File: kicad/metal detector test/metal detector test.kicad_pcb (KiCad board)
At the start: 2 copper layers, 0 parts

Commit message: Starting PCB layout.  Also added alternate MPNs for a few more regulators sampled from TI
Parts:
- added BT1: 12V (18650 x3), Connector_PinHeader_2.54mm:PinHeader_1x02_P2.54mm_Vertical, F.Cu at (137.2, 95.9)
- added C1: 100u, Capacitor_SMD:C_1206_3216Metric_Pad1.33x1.80mm_HandSolder, F.Cu at (74.0, 122.0)
- added C10: 100n, Capacitor_SMD:C_0805_2012Metric_Pad1.18x1.45mm_HandSolder, F.Cu at (143.5, 95.2)
- added C11: 3.3u, Capacitor_SMD:C_0805_2012Metric_Pad1.18x1.45mm_HandSolder, F.Cu at (151.1, 95.2)
- added C12: 10u, Capacitor_SMD:C_1206_3216Metric_Pad1.33x1.80mm_HandSolder, F.Cu at (135.9, 99.1)
- added C13: 100n, Capacitor_SMD:C_0805_2012Metric_Pad1.18x1.45mm_HandSolder, F.Cu at (201.0, 90.5)
- added C14: 100n, Capacitor_SMD:C_0805_2012Metric_Pad1.18x1.45mm_HandSolder, F.Cu at (197.2, 98.7)
- added C15: 1000u, Capacitor_THT:CP_Radial_D10.0mm_P5.00mm, F.Cu at (192.6, 111.4)
- added C16: 100n, Capacitor_SMD:C_0805_2012Metric_Pad1.18x1.45mm_HandSolder, F.Cu at (192.3, 101.9)
- added C17: 100u, Capacitor_SMD:C_1206_3216Metric_Pad1.33x1.80mm_HandSolder, F.Cu at (201.0, 100.0)
- added C18: 100n, Capacitor_SMD:C_0805_2012Metric_Pad1.18x1.45mm_HandSolder, F.Cu at (194.6, 90.5)
- added C19: .33u, Capacitor_SMD:C_0805_2012Metric_Pad1.18x1.45mm_HandSolder, F.Cu at (137.2, 103.5)
- added C2: 470n, Capacitor_SMD:C_1206_3216Metric_Pad1.33x1.80mm_HandSolder, F.Cu at (149.2, 121.9)
- added C20: 100n, Capacitor_SMD:C_0805_2012Metric_Pad1.18x1.45mm_HandSolder, F.Cu at (143.5, 106.7)
- added C21: 3.3u, Capacitor_SMD:C_0805_2012Metric_Pad1.18x1.45mm_HandSolder, F.Cu at (151.1, 106.7)
- added C22: 1000u, Capacitor_THT:CP_Radial_D10.0mm_P5.00mm, F.Cu at (205.0, 96.2)
- added C23: 100n, Capacitor_SMD:C_0805_2012Metric_Pad1.18x1.45mm_HandSolder, F.Cu at (158.1, 156.2)
- added C24: 100n, Capacitor_SMD:C_0805_2012Metric_Pad1.18x1.45mm_HandSolder, F.Cu at (209.9, 103.2)
- added C25: 1000u, Capacitor_THT:CP_Radial_D10.0mm_P5.00mm, F.Cu at (213.1, 112.9)
- added C26: 33n, Capacitor_SMD:C_0805_2012Metric_Pad1.18x1.45mm_HandSolder, F.Cu at (154.9, 164.5)
- added C27: 100n, Capacitor_SMD:C_0805_2012Metric_Pad1.18x1.45mm_HandSolder, F.Cu at (209.9, 106.4)
- added C28: 100n, Capacitor_SMD:C_0805_2012Metric_Pad1.18x1.45mm_HandSolder, F.Cu at (164.5, 156.2)
- added C29: 100n, Capacitor_SMD:C_0805_2012Metric_Pad1.18x1.45mm_HandSolder, F.Cu at (166.4, 160.0)
- added C3: 22u, Capacitor_SMD:C_1206_3216Metric_Pad1.33x1.80mm_HandSolder, F.Cu at (149.2, 132.1)
- added C30: 100n, Capacitor_SMD:C_0805_2012Metric_Pad1.18x1.45mm_HandSolder, F.Cu at (166.4, 168.9)
- added C4: 100n, Capacitor_SMD:C_0805_2012Metric_Pad1.18x1.45mm_HandSolder, F.Cu at (115.0, 172.0)
- added C5: 100n, Capacitor_SMD:C_0805_2012Metric_Pad1.18x1.45mm_HandSolder, F.Cu at (75.2, 25.4)
- added C6: 100n, Capacitor_SMD:C_0805_2012Metric_Pad1.18x1.45mm_HandSolder, F.Cu at (77.0, 127.0)
- added C7: 33n, Capacitor_SMD:C_0805_2012Metric_Pad1.18x1.45mm_HandSolder, F.Cu at (110.0, 163.0)
- added C8: 10n, Capacitor_SMD:C_0805_2012Metric_Pad1.18x1.45mm_HandSolder, F.Cu at (103.0, 171.0)
- added C9: .33u, Capacitor_SMD:C_0805_2012Metric_Pad1.18x1.45mm_HandSolder, F.Cu at (137.2, 92.1)
- added DS1: 2.42_inch_128x64_oled, allen footprints:oled_2.42in_128x64, F.Cu at (81.3, 22.9)
- added FB1: ~, Inductor_SMD:L_0805_2012Metric_Pad1.05x1.20mm_HandSolder, F.Cu at (74.9, 27.9)
- added G***: LOGO, LOGO, F.Cu at (36.8, 184.8)
- added H1: MountingHole, MountingHole:MountingHole_3.7mm, F.Cu at (121.9, 55.9)
- added H2: MountingHole, MountingHole:MountingHole_3.7mm, F.Cu at (55.9, 55.9)
- added H3: MountingHole, MountingHole:MountingHole_3.7mm, F.Cu at (55.9, 172.7)
- added H4: MountingHole, MountingHole:MountingHole_3.7mm, F.Cu at (132.1, 188.0)
- added J1: 3.5mm audio jack TRS, allen footprints:SJ-3524-SMT_audio_jack_with_tip_switch_smt, F.Cu at (217.2, 126.7)
- added JP1: SolderJumper_2_Open, Jumper:SolderJumper-2_P1.3mm_Open_Pad1.0x1.5mm, F.Cu at (174.6, 57.8)
- added JP2: SolderJumper_2_Open, Jumper:SolderJumper-2_P1.3mm_Open_Pad1.0x1.5mm, F.Cu at (71.8, 30.5)
- added JP3: SolderJumper_2_Open, Jumper:SolderJumper-2_P1.3mm_Open_Pad1.0x1.5mm, F.Cu at (75.6, 30.5)
- added JP4: SolderJumper_2_Open, Jumper:SolderJumper-2_P1.3mm_Open_Pad1.0x1.5mm, F.Cu at (154.3, 57.8)
- added LS1: Speaker, Connector_PinHeader_2.54mm:PinHeader_1x02_P2.54mm_Vertical, F.Cu at (204.2, 132.4)
- added L_RX1: 6m1, Connector_PinHeader_2.54mm:PinHeader_1x02_P2.54mm_Vertical, F.Cu at (151.8, 163.2)
- added L_TX1: 5m6, Connector_PinHeader_2.54mm:PinHeader_1x02_P2.54mm_Vertical, F.Cu at (105.0, 163.0)
- added L_TX2: 5m6, Connector_PinHeader_2.54mm:PinHeader_1x02_P2.54mm_Vertical, F.Cu at (188.3, 119.7)
- added Q1: ~, allen footprints:SOT-89-3_Handsoldering_allen, F.Cu at (117.0, 158.0)
- added Q2: ~, allen footprints:SOT-89-3_Handsoldering_allen, F.Cu at (117.0, 166.0)
- added R1: 27k, Resistor_SMD:R_0805_2012Metric_Pad1.20x1.40mm_HandSolder, F.Cu at (124.0, 165.0)
- added R10: 33k, Resistor_SMD:R_0805_2012Metric_Pad1.20x1.40mm_HandSolder, F.Cu at (68.0, 78.0)
- added R11: 2k, Resistor_SMD:R_0805_2012Metric_Pad1.20x1.40mm_HandSolder, F.Cu at (125.0, 173.0)
- added R12: 10k, Resistor_SMD:R_0805_2012Metric_Pad1.20x1.40mm_HandSolder, F.Cu at (194.6, 96.2)
- added R13: 2.7, Resistor_SMD:R_0805_2012Metric_Pad1.20x1.40mm_HandSolder, F.Cu at (192.3, 104.5)
- added R14: 50k, Resistor_SMD:R_0805_2012Metric_Pad1.20x1.40mm_HandSolder, F.Cu at (161.9, 160.0)
- added R15: 5k1, Resistor_SMD:R_0805_2012Metric_Pad1.20x1.40mm_HandSolder, F.Cu at (158.1, 163.2)
- added R16: 2.7, Resistor_SMD:R_0805_2012Metric_Pad1.20x1.40mm_HandSolder, F.Cu at (209.9, 108.9)
- added R17: 5k1, Resistor_SMD:R_0805_2012Metric_Pad1.20x1.40mm_HandSolder, F.Cu at (158.1, 165.7)
- added R18: 50k, Resistor_SMD:R_0805_2012Metric_Pad1.20x1.40mm_HandSolder, F.Cu at (161.9, 168.9)
- added R19: 100k, Resistor_SMD:R_0805_2012Metric_Pad1.20x1.40mm_HandSolder, F.Cu at (170.2, 163.6)
- added R2: 1.2k, Resistor_SMD:R_0805_2012Metric_Pad1.20x1.40mm_HandSolder, F.Cu at (124.0, 169.0)
- added R20: 100k, Resistor_SMD:R_0805_2012Metric_Pad1.20x1.40mm_HandSolder, F.Cu at (170.2, 167.4)
- added R3: 560, Resistor_SMD:R_0805_2012Metric_Pad1.20x1.40mm_HandSolder, F.Cu at (124.0, 161.0)
- added R4: 18k, Resistor_SMD:R_0805_2012Metric_Pad1.20x1.40mm_HandSolder, F.Cu at (79.0, 115.0)
- added R5: 100k, Resistor_SMD:R_0805_2012Metric_Pad1.20x1.40mm_HandSolder, F.Cu at (80.0, 156.0)
- added R6: 100k, Resistor_SMD:R_0805_2012Metric_Pad1.20x1.40mm_HandSolder, F.Cu at (89.0, 121.0)
- added R7: 100k, Resistor_SMD:R_0805_2012Metric_Pad1.20x1.40mm_HandSolder, F.Cu at (67.0, 74.0)
- added R8: 18k, Resistor_SMD:R_0805_2012Metric_Pad1.20x1.40mm_HandSolder, F.Cu at (72.0, 127.0)
- added R9: 12k, Resistor_SMD:R_0805_2012Metric_Pad1.20x1.40mm_HandSolder, F.Cu at (124.0, 157.0)
- added SW0: SW_SPST, allen footprints:SW_SPST_PTS647, F.Cu at (261.0, 109.6)
- added SW1: SW_SPST, allen footprints:SW_SPST_PTS647, F.Cu at (268.6, 109.6)
- added SW2: SW_SPST, allen footprints:SW_SPST_PTS647, F.Cu at (276.2, 109.6)
- added SW3: SW_SPST, allen footprints:SW_SPST_PTS647, F.Cu at (276.2, 118.5)
- added SW4: SW_SPST, allen footprints:SW_SPST_PTS647, F.Cu at (283.8, 118.5)
- added SW5: SW_SPST, allen footprints:SW_SPST_PTS647, F.Cu at (291.5, 118.5)
- added SW6: SW_SPST, allen footprints:SW_SPST_PTS647, F.Cu at (291.5, 109.6)
- added SW7: SW_SPST, allen footprints:SW_SPST_PTS647, F.Cu at (299.1, 109.6)
- added SW8: SW_SPST, allen footprints:SW_SPST_PTS647, F.Cu at (306.7, 109.6)
- added TP1: 1.6v, TestPoint:TestPoint_Pad_D1.5mm, F.Cu at (163.8, 171.4)
- added TP2: RX_RAW, TestPoint:TestPoint_Pad_D1.5mm, F.Cu at (158.1, 160.0)
- added TP3: RX_FILT, TestPoint:TestPoint_Pad_D1.5mm, F.Cu at (164.5, 151.8)
- added TP4: TX_A_RAW, TestPoint:TestPoint_Pad_D1.5mm, F.Cu at (43.8, 91.8)
- added TP5: TX_A_SCALED, TestPoint:TestPoint_Pad_D1.5mm, F.Cu at (43.8, 95.4)
- added TP6: TX_D_RAW, TestPoint:TestPoint_Pad_D1.5mm, F.Cu at (197.8, 86.0)
- added TP7: TX_D_FILT, TestPoint:TestPoint_Pad_D1.5mm, F.Cu at (192.1, 97.5)
- added TP8: TX_D_AMP, TestPoint:TestPoint_Pad_D1.5mm, F.Cu at (185.1, 117.2)
- added U1: 9v lin reg, Package_TO_SOT_SMD:SOT-223-3_TabPin2, F.Cu at (151.1, 127.0)
- added U10: 3.3v lin reg, Package_TO_SOT_SMD:SOT-223-3_TabPin2, F.Cu at (149.9, 101.0)
- added U11: lp filter, Package_SO:TSSOP-8_4.4x3mm_P0.65mm, F.Cu at (161.3, 154.3)
- added U12: ~, Package_SO:SOIC-8_3.9x4.9mm_P1.27mm, F.Cu at (164.5, 164.5)
- added U2: ~, Package_SO:SOIC-8_3.9x4.9mm_P1.27mm, F.Cu at (82.0, 121.0)
- added U3: nucleo-32 uC module, allen footprints:Nucleo-32_allen, F.Cu at (184.9, 38.7)
- added U4: 5v lin reg, Package_TO_SOT_SMD:SOT-223-3_TabPin2, F.Cu at (142.2, 89.5)
- added U5: 3.3v lin reg, Package_TO_SOT_SMD:SOT-223-3_TabPin2, F.Cu at (149.9, 89.5)
- added U6: audio amp, Package_TO_SOT_SMD:TO-263-7_TabPin4, F.Cu at (201.6, 114.0)
- added U7: lp filter, Package_SO:TSSOP-8_4.4x3mm_P0.65mm, F.Cu at (197.8, 92.4)
- added U8: switch debounce, Package_SO:SOIC-20W_7.5x12.8mm_P1.27mm, F.Cu at (283.8, 99.9)
- added U9: 5v lin reg, Package_TO_SOT_SMD:SOT-223-3_TabPin2, F.Cu at (142.2, 101.0)
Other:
- board outline added: 76.2 x 127 mm

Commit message: Working on pcb layout, generated BOM
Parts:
- added FID1: Fiducial, Fiducial:Fiducial_0.5mm_Mask1.5mm, F.Cu at (41.9, 76.2)
- added FID2: Fiducial, Fiducial:Fiducial_0.5mm_Mask1.5mm, F.Cu at (41.9, 79.2)
- added FID3: Fiducial, Fiducial:Fiducial_0.5mm_Mask1.5mm, F.Cu at (41.9, 82.3)
- added H5: Strain Rel, MountingHole:MountingHole_3.2mm_M3, F.Cu at (35.6, 113.3)
- added H6: Strain Rel, MountingHole:MountingHole_3.2mm_M3, F.Cu at (116.9, 173.2)
- added H7: Strain Rel, MountingHole:MountingHole_3.2mm_M3, F.Cu at (141.0, 146.6)
- added H8: Strain Rel, MountingHole:MountingHole_3.2mm_M3, F.Cu at (69.6, 109.2)
- added H9: Strain Rel, MountingHole:MountingHole_3.2mm_M3, F.Cu at (141.7, 153.2)
- added LS2: SMT Speaker, allen footprints:CDS-13138-SMT-TR_speaker_smt, F.Cu at (168.2, 138.0)
- added SW9: SW_SPST, allen footprints:A11AH_right_angle_toggle_switch, F.Cu at (66.2, 149.0)
- C1, C12, C17, C3: footprint Capacitor_SMD:C_1206_3216Metric_Pad1.33x1.80mm_HandSolder -> allen footprints:C_Polarized_1206_3216Metric_HandSolder_allen
- C11, C21: footprint Capacitor_SMD:C_0805_2012Metric_Pad1.18x1.45mm_HandSolder -> allen footprints:C_Polarized_0805_2012Metric_HandSolder_allen
- DS1, G***, SW0, SW1, SW2, SW3, SW4, SW5, SW6, SW7, SW8, U8: moved to B.Cu
- FB1: value ~ -> ferrite bead smt
- LS1: value Speaker -> Ext. Speaker
- Q1: value ~ -> PNP
- Q2: value ~ -> NPN
- R14, R18: value 50k -> 49.9k
- U12: value ~ -> op amp (lower voltage)
- U2: value ~ -> op amp (higher voltage)
- moved SW8 164.5 mm to (142.9, 94.7), turned to 180 degrees
- moved SW7 149.3 mm to (150.5, 94.7), turned to 180 degrees
- moved SW5 134.2 mm to (158.1, 103.6), turned to 180 degrees
- moved SW6 134.2 mm to (158.1, 94.7), turned to 180 degrees
- moved TP1 119.4 mm to (58.7, 114.8), turned to -90 degrees
- moved SW4 119.0 mm to (165.7, 103.6), turned to 180 degrees
- moved U8 119.0 mm to (165.7, 85.0)
- moved R20 117.1 mm to (60.3, 126.7), turned to 180 degrees
- moved C30 117.0 mm to (58.8, 122.9), turned to 90 degrees
- moved R18 114.8 mm to (58.8, 118.5), turned to -90 degrees
- moved U3 113.4 mm to (73.7, 60.8), turned to 0 degrees
- moved R19 112.2 mm to (64.2, 126.7), turned to 180 degrees
- moved DS1 112.1 mm to (193.0, 31.4), turned to -90 degrees
- moved U12 110.1 mm to (63.2, 121.0), turned to -90 degrees
- moved R17 108.9 mm to (62.0, 114.7), turned to -90 degrees
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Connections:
- BT1 pad 1: +BATT -> Net-(BT1-+)

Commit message: slow progress
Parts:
- added JP5: SolderJumper_2_Open_big, allen footprints:SolderJumper-2_Open_big_allen, F.Cu at (119.4, 159.0)
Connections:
- C1 pad 1: +9V -> Net-(JP5-B)
- R1 pad 1: +9V -> Net-(JP5-B)
- R2 pad 1: +9V -> Net-(JP5-B)
- R3 pad 1: +9V -> Net-(JP5-B)
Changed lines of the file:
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@@
   (net 74 "Net-(U12B--)")
   (net 75 "Net-(DS1-VCC)")
+  (net 76 "Net-(JP5-B)")
   (footprint "Resistor_SMD:R_0805_2012Metric_Pad1.20x1.40mm_HandSolder" placed (layer "F.Cu")
     (at 60.341 126.746 180)
@@
       (stroke (width 0.1) (type solid)) (layer "F.Fab"))
     (pad "1" smd roundrect (at -1 0 270) (size 1.2 1.4) (layers "F.Cu" "F.Paste" "F.Mask") (roundrect_rratio 0.208333)
-      (net 3 "+9V") (pintype "passive"))
+      (net 76 "Net-(JP5-B)") (pintype "passive"))
     (pad "2" smd roundrect (at 1 0 270) (size 1.2 1.4) (layers "F.Cu" "F.Paste" "F.Mask") (roundrect_rratio 0.208333)
       (net 39 "Net-(Q2-B)") (pintype "passive"))
@@
     )
   )
+  (footprint "allen footprints:SolderJumper-2_Open_big_allen" (layer "F.Cu")
+    (at 119.38 159.004 180)
+    (descr "SMD Solder Jumper open big")
+    (tags "solder jumper open")
+    (property "MPN" "")
+    (property "Sheetfile" "metal detector test.kicad_sch")
+    (property "Sheetname" "")
+    (property "ki_description" "Solder Jumper, 2-pole, open")
+    (property "ki_keywords" "solder jumper SPST")
+    (attr exclude_from_pos_files)
+    (fp_text reference "JP5" (at 0.508 -1.905) (layer "F.SilkS")
+        (effects (font (size 1 1) (thickness 0.15)))
+    )
+    (fp_text value "SolderJumper_2_Open_big" (at 0 1.9) (layer "F.Fab") hide
+        (effects (font (size 1 1) (thickness 0.15)))
+    )
+    (fp_line (start -1.4 -1.1524) (end 1.4 -1.1524)
+      (stroke (width 0.12) (type solid)) (layer "F.SilkS"))
+    (fp_line (start -1.4 1.1524) (end -1.4 -1.1524)
+      (stroke (width 0.12) (type solid)) (layer "F.SilkS"))
+    (fp_line (start 1.4 -1.1524) (end 1.4 1.1524)
+      (stroke (width 0.12) (type solid)) (layer "F.SilkS"))
+    (fp_line (start 1.4 1.1524) (end -1.4 1.1524)
+      (stroke (width 0.12) (type solid)) (layer "F.SilkS"))
+    (fp_line (start -1.65 -1.25) (end -1.65 1.25)
+      (stroke (width 0.05) (type solid)) (layer "F.CrtYd"))
+    (fp_line (start -1.65 -1.25) (end 1.65 -1.25)
+      (stroke (width 0.05) (type solid)) (layer "F.CrtYd"))
+    (fp_line (start 1.65 1.25) (end -1.65 1.25)
+      (stroke (width 0.05) (type solid)) (layer "F.CrtYd"))
+    (fp_line (start 1.65 1.25) (end 1.65 -1.25)
+      (stroke (width 0.05) (type solid)) (layer "F.CrtYd"))
+    (pad "1" smd rect (at -0.65 0 180) (size 1 2.032) (layers "F.Cu" "F.Mask")
+      (net 3 "+9V") (pinfunction "A") (pintype "passive"))
+    (pad "2" smd rect (at 0.65 0 180) (size 1 2.032) (layers "F.Cu" "F.Mask")
+      (net 76 "Net-(JP5-B)") (pinfunction "B") (pintype "passive"))
+  )
   (footprint "Capacitor_SMD:C_0805_2012Metric_Pad1.18x1.45mm_HandSolder" placed (layer "F.Cu")
     (at 71.501 121.031 180)
@@
       (stroke (width 0.1) (type solid)) (layer "F.Fab"))
     (pad "1" smd roundrect (at -1 0 270) (size 1.2 1.4) (layers "F.Cu" "F.Paste" "F.Mask") (roundrect_rratio 0.208333)
-      (net 3 "+9V") (pintype "passive"))
+      (net 76 "Net-(JP5-B)") (pintype "passive"))
     (pad "2" smd roundrect (at 1 0 270) (size 1.2 1.4) (layers "F.Cu" "F.Paste" "F.Mask") (roundrect_rratio 0.208333)
       (net 38 "Net-(Q1-E)") (pintype "passive"))
@@
       (stroke (width 0.1) (type solid)) (layer "F.Fab"))
     (pad "1" smd roundrect (at -1 0 270) (size 1.2 1.4) (layers "F.Cu" "F.Paste" "F.Mask") (roundrect_rratio 0.208333)
-      (net 3 "+9V") (pintype "passive"))
+      (net 76 "Net-(JP5-B)") (pintype "passive"))
     (pad "2" smd roundrect (at 1 0 270) (size 1.2 1.4) (layers "F.Cu" "F.Paste" "F.Mask") (roundrect_rratio 0.208333)
       (net 37 "Net-(Q1-B)") (pintype "passive"))
@@
       (stroke (width 0.1) (type solid)) (layer "F.Fab"))
     (pad "1" smd roundrect (at -1.5625 0 270) (size 1.325 1.8) (layers "F.Cu" "F.Paste" "F.Mask") (roundrect_rratio 0.188679)
-      (net 3 "+9V") (pintype "passive"))
+      (net 76 "Net-(JP5-B)") (pintype "passive"))
     (pad "2" smd roundrect (at 1.5625 0 270) (size 1.325 1.8) (layers "F.Cu" "F.Paste" "F.Mask") (roundrect_rratio 0.188679)
       (net 2 "GNDA") (pintype "passive"))

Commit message: Added holes on corners of OLED footprint after carefully measuring twice, working on layout still.
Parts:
- moved TP3 201.5 mm to (268.0, 60.1)
- moved C26 201.5 mm to (255.3, 50.5)
- moved C30 201.5 mm to (250.8, 62.0)
- moved H8 201.5 mm to (261.6, 48.3)
- moved L_RX1 201.5 mm to (256.5, 47.4)
- moved R15 201.5 mm to (256.5, 53.7)
- moved R17 201.5 mm to (254.0, 53.7)
- moved R18 201.5 mm to (250.8, 57.5)
- moved R19 201.5 mm to (256.2, 65.8)
- moved R20 201.5 mm to (252.4, 65.8)
- moved TP1 201.5 mm to (250.7, 53.8)
- moved U11 201.5 mm to (265.4, 56.9)
- moved U12 201.5 mm to (255.3, 60.1)
- moved C23 201.5 mm to (263.5, 53.7)
- moved C28 201.5 mm to (263.5, 60.1)
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
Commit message: Making custom mounting / strain relief holes
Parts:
- added C12: 100n, Capacitor_SMD:C_0805_2012Metric_Pad1.18x1.45mm_HandSolder, B.Cu at (173.7, 85.3)
- H1, H2, H3, H4: value MountingHole -> Strain Rel; footprint MountingHole:MountingHole_3.7mm -> allen footprints:mounting_hole_3mm
- H5: footprint MountingHole:MountingHole_3.2mm_M3 -> allen footprints:mounting_hole_3mm
- H6, H7, H8, H9: value Strain Rel -> MountingHole; footprint MountingHole:MountingHole_3.2mm_M3 -> allen footprints:mounting_hole_4-40_thru
- moved H3 192.6 mm to (182.6, 38.0)
- moved H5 161.7 mm to (182.6, 46.0)
- moved H4 143.6 mm to (182.6, 42.0)
- moved H6 140.1 mm to (178.5, 34.1)
- moved H2 136.1 mm to (182.6, 34.0)
- moved H7 114.5 mm to (178.5, 38.4)
- moved H9 112.4 mm to (178.5, 46.9)
- moved DS1 98.8 mm to (95.2, 39.2)
- moved C11 96.1 mm to (122.7, 192.1), turned to 180 degrees
- moved U5 95.1 mm to (121.4, 186.4), turned to 90 degrees
- moved H8 83.3 mm to (178.5, 42.6), turned to 0 degrees
- moved C20 64.7 mm to (27.3, 149.9)
- moved C21 64.7 mm to (27.3, 146.1)
- moved U9 64.7 mm to (21.4, 147.8)
- moved H1 48.5 mm to (182.6, 29.5)
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- renumbered C12 to C13, C13 to C14, C14 to C15, C15 to C16, C16 to C17, C17 to C18, C18 to C19, C4 to C2, C19 to C20, C20 to C21, C21 to C22, C22 to C23, C23 to C24, C24 to C25, C25 to C26, C26 to C27, C27 to C28, C28 to C29, C5 to C3, C29 to C30, C30 to C31, C6 to C4, C7 to C5, C8 to C6, C2 to C7, C3 to C8, JP5 to JP1, JP1 to JP2, JP2 to JP3, JP3 to JP4, JP4 to JP5, LS2 to LS1, LS1 to LS2, SW9 to SW1, SW8 to SW10, SW0 to SW2, SW1 to SW3, SW2 to SW4, SW3 to SW5, SW4 to SW6, SW5 to SW7, SW6 to SW8, SW7 to SW9, TP5 to TP1, TP4 to TP2, TP8 to TP3, TP6 to TP4, TP7 to TP5, TP2 to TP6, TP3 to TP7, TP1 to TP8, U2 to U1, U3 to U2, U1 to U3
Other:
- board outline removed
- board text added: "3.3V(RX)"
- board text added: "3.3V(TX)"
- board text added: "9V(TX)"

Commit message: making progress on pcb layout
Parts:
- moved TP7 228.4 mm to (50.0, 128.5)
- moved TP6 218.6 mm to (50.8, 118.1)
- moved C23 202.7 mm to (72.3, 120.8), turned to 90 degrees
- moved U11 199.8 mm to (75.5, 118.9), turned to 90 degrees
- moved C26 199.2 mm to (67.9, 118.1)
- moved C31 199.2 mm to (63.4, 129.5)
- moved L_RX1 199.2 mm to (69.1, 114.9)
- moved R15 199.2 mm to (69.1, 121.2)
- moved R17 199.2 mm to (66.6, 121.2)
- moved R18 199.2 mm to (63.4, 125.0)
- moved R19 199.2 mm to (68.8, 133.3)
- moved R20 199.2 mm to (65.0, 133.3)
- moved TP8 199.2 mm to (63.3, 121.4)
- moved U12 199.2 mm to (67.9, 127.6)
- moved C30 199.2 mm to (72.3, 129.5)
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- renumbered C23 to C12, C12 to C13, C13 to C14, C14 to C15, C15 to C16, C16 to C17, C17 to C18, C24 to C23, C25 to C24, C26 to C25, C27 to C26, C28 to C27, C29 to C28, C18 to C29
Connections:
- C16 pad 1: Net-(U6A-+) -> Net-(U6B-+)
- C17 pad 1: Net-(C16-Pad1) -> Net-(C17-Pad1)
- C24 pad 1: Net-(U6B-+) -> Net-(U6A-+)
- C25 pad 1: Net-(C26-Pad1) (its old number) -> Net-(C25-Pad1)
- LS1 pad 1: GNDA -> Net-(J1-PadTN)
- LS1 pad 2: Net-(J1-PadTN) -> GNDA
- R13 pad 1: Net-(C16-Pad1) -> Net-(C17-Pad1)
- R16 pad 1: Net-(C26-Pad1) (its old number) -> Net-(C25-Pad1)
- SW1 pad 1: +BATT -> Net-(BT1-+)
- SW1 pad 2: Net-(BT1-+) -> +BATT
- U6 pad 1: Net-(C26-Pad1) (its old number) -> Net-(C17-Pad1)
- U6 pad 7: Net-(C16-Pad1) -> Net-(C25-Pad1)

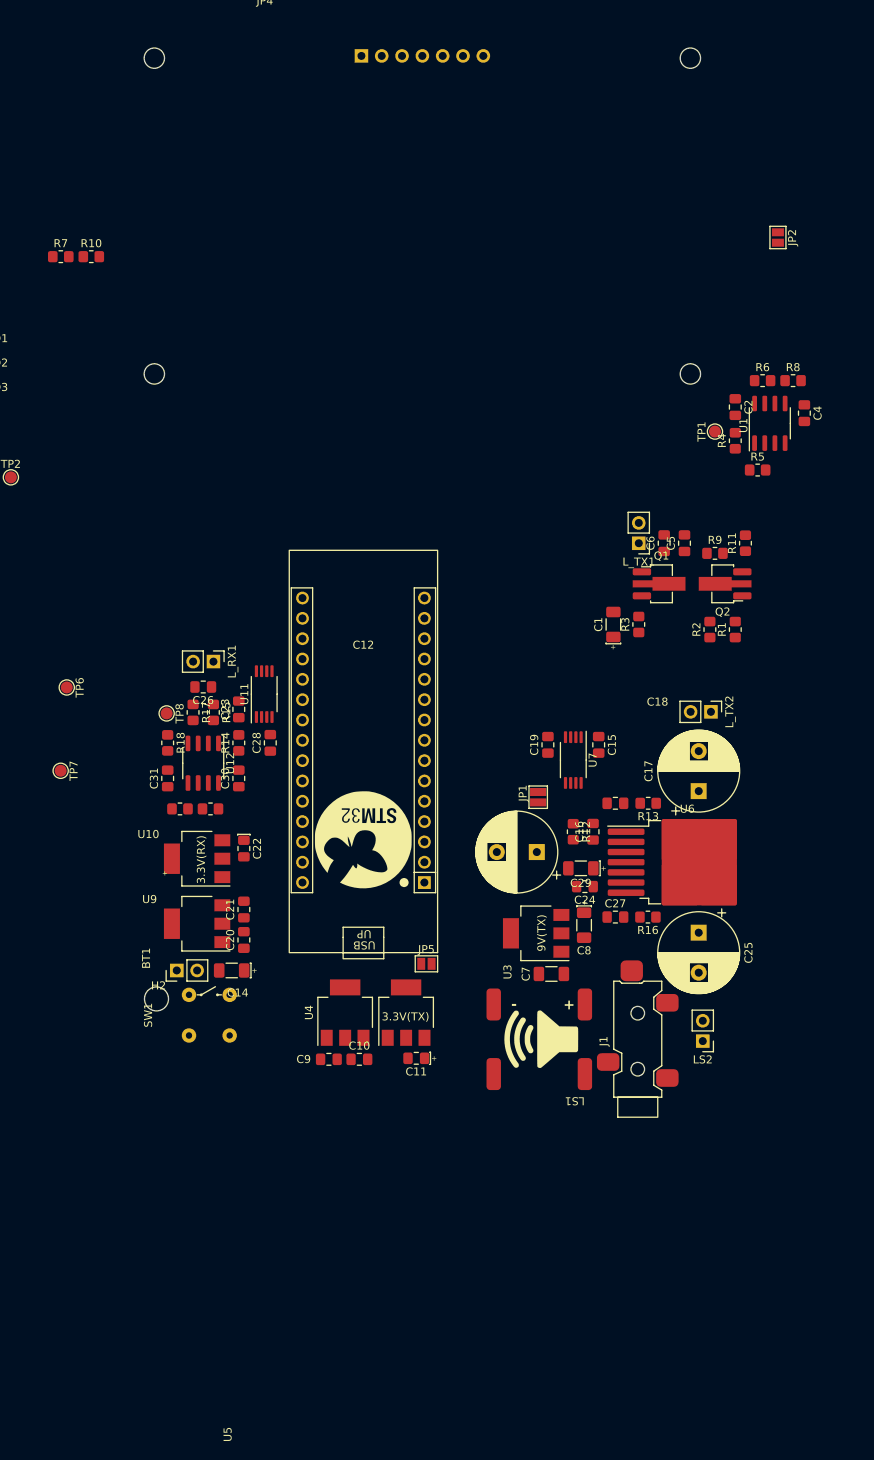
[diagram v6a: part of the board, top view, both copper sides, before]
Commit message: Mostly positioned the parts
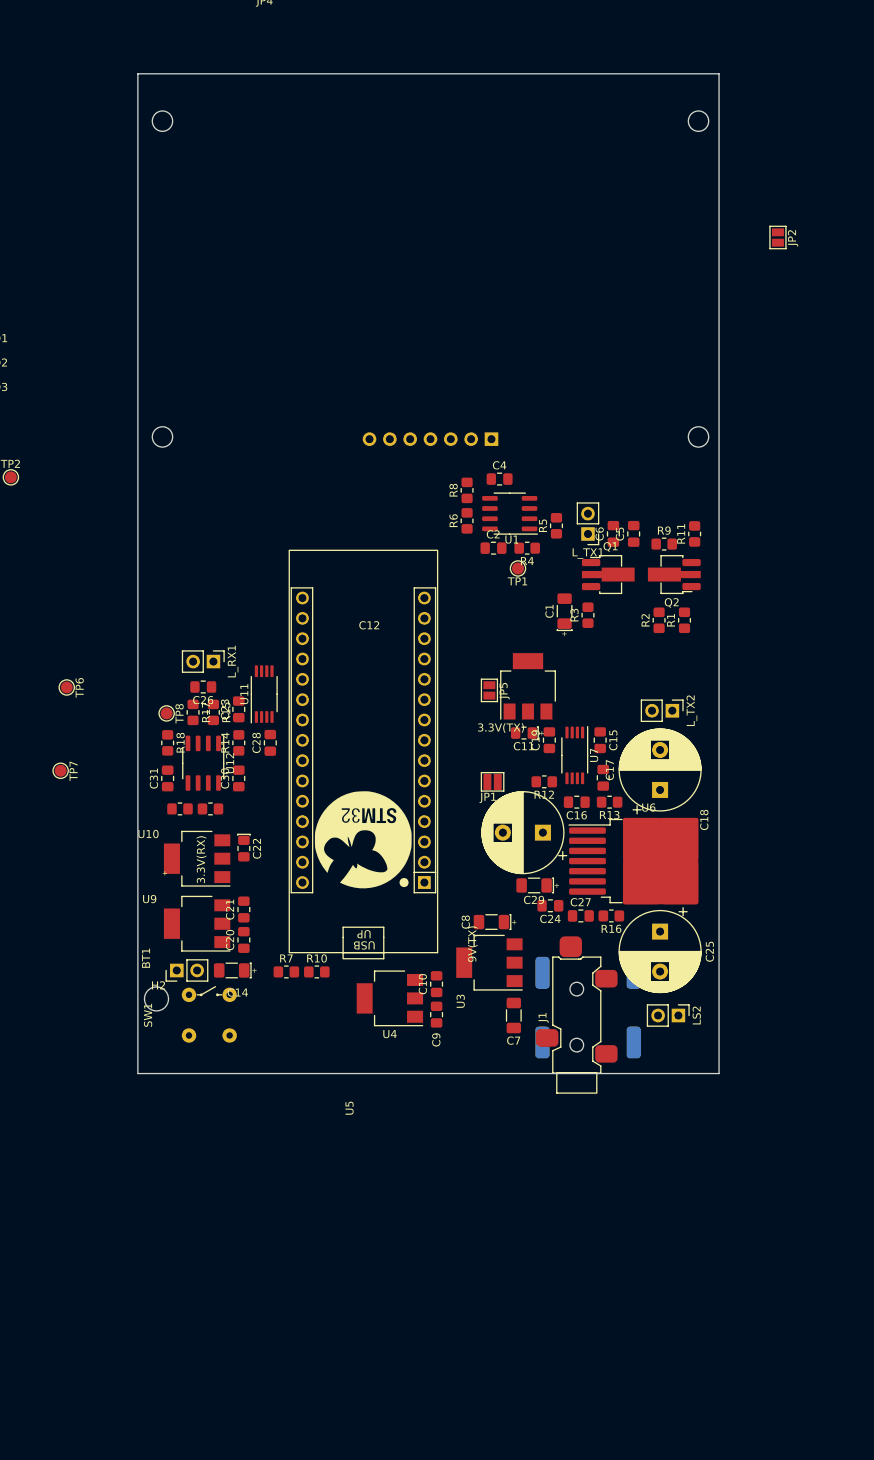
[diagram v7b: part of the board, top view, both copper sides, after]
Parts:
- LS1: moved to B.Cu
- moved R10 93.7 mm to (82.1, 153.7)
- moved R7 93.7 mm to (78.2, 153.7)
- moved DS1 47.9 mm to (96.3, 87.1), turned to 90 degrees
- moved U5 43.5 mm to (108.5, 118.0)
- moved R8 43.0 mm to (100.8, 93.5), turned to 90 degrees
- moved C11 42.8 mm to (108.0, 123.8)
- moved R6 40.9 mm to (100.8, 97.3), turned to 90 degrees
- moved C4 39.0 mm to (104.9, 92.1), turned to 0 degrees
- moved JP5 35.1 mm to (103.6, 118.5), turned to -90 degrees
- moved C2 35.0 mm to (104.1, 100.7), turned to 0 degrees
- moved U1 34.4 mm to (106.2, 96.4), turned to 180 degrees
- moved TP1 30.0 mm to (107.2, 103.2), turned to 180 degrees
- moved R4 29.3 mm to (108.4, 100.7), turned to 180 degrees
- moved R5 26.1 mm to (112.0, 97.9), turned to 90 degrees
- moved C9 14.6 mm to (97.0, 159.0), turned to 90 degrees
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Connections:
- C2 pad 1: +9V -> Net-(JP1-B)
- R6 pad 1: +9V -> Net-(JP1-B)
- U1 pad 8: +9V -> Net-(JP1-B)
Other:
- board outline added: 72.6 x 125 mm
